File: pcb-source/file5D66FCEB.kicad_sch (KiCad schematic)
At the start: 9 parts, among them J5 Conn_01x02_Female, U3 AZ1117-5.0, U7 AMS1117-3.3, U8 AMS1117-1.8

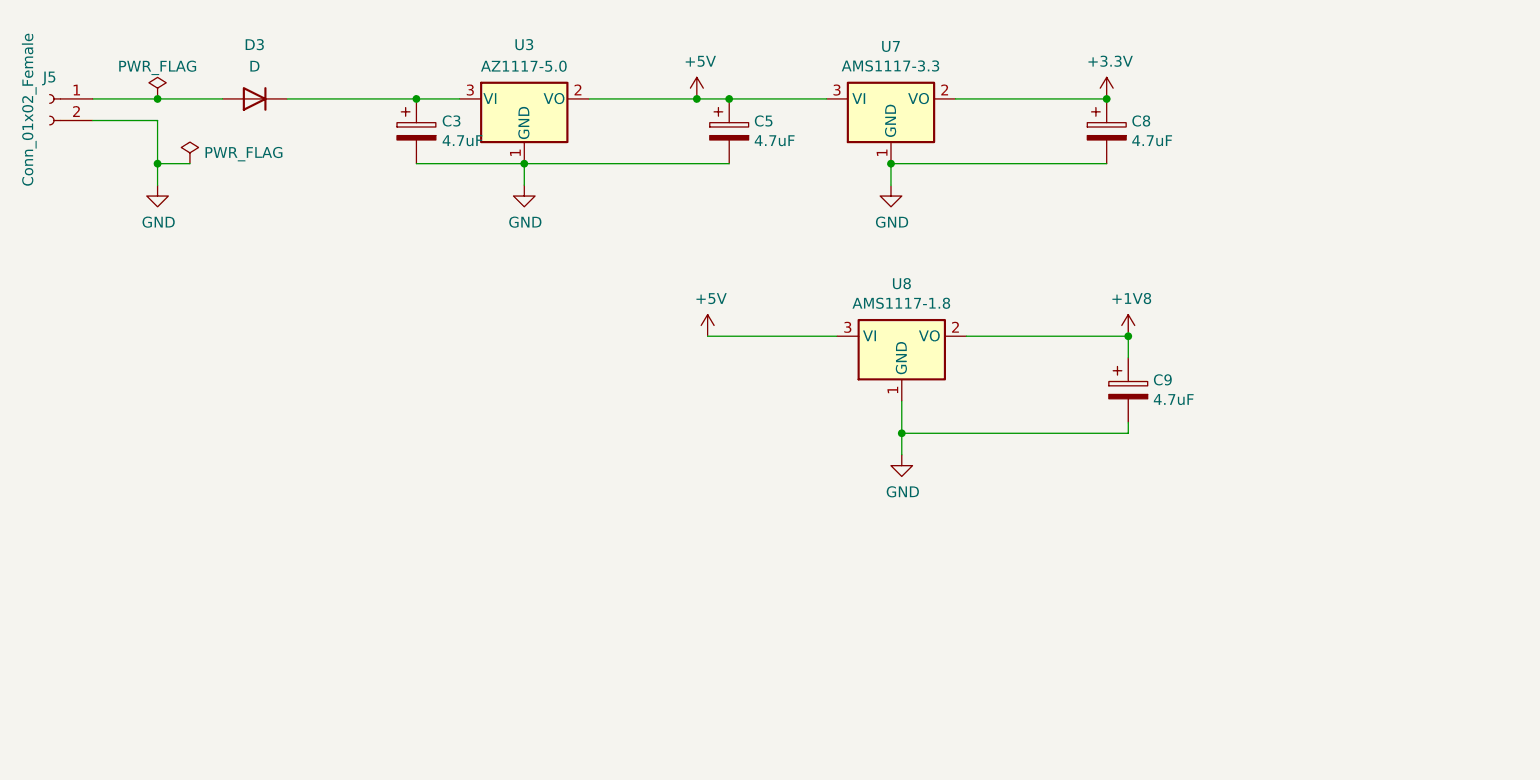
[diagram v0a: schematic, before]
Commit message: 1.2 version with 2 SPI buses
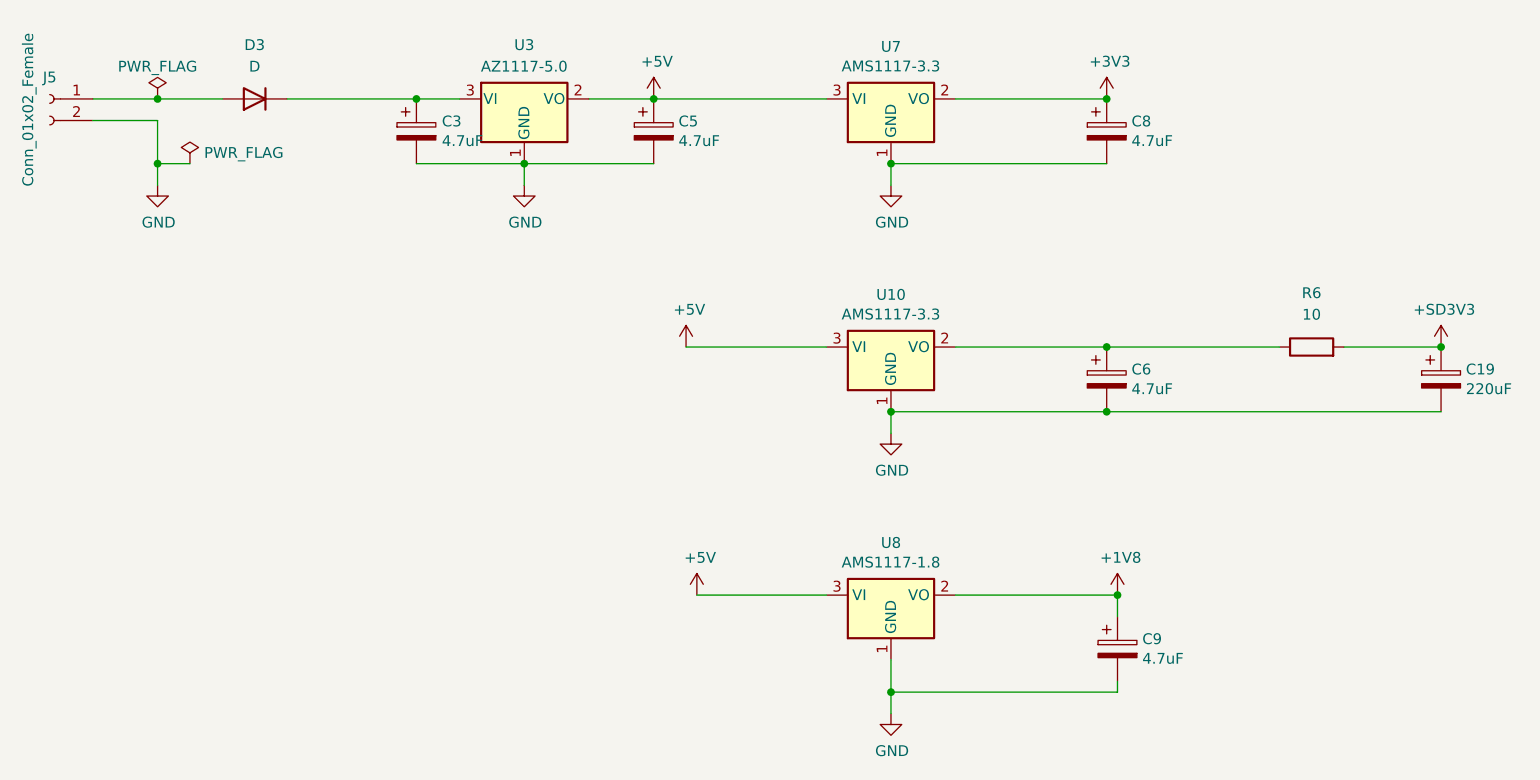
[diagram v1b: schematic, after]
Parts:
- added C19: 220uF, Capacitor_THT:CP_Radial_D6.3mm_P2.50mm, symbol AtariHDisk4-rescue:CP-Device
- added C6: 4.7uF, Capacitor_SMD:C_1206_3216Metric, symbol AtariHDisk4-rescue:CP-Device
- added R6: 10, Resistor_SMD:R_0805_2012Metric, symbol Device:R
- added U10: AMS1117-3.3, Package_TO_SOT_SMD:SOT-223-3_TabPin2, symbol Regulator_Linear:AMS1117-3.3
- C3: footprint Capacitor_THT:CP_Radial_D5.0mm_P2.00mm -> Capacitor_THT:CP_Radial_D6.3mm_P2.50mm
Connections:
- net +5V: now also U10.3 (VI)
- net GND: now also C19.2, C6.2, U10.1 (GND)
- new net: C6.1, R6.1, U10.2 (VO)
- new net +SD3V3: C19.1, R6.2
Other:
- moved on the sheet: C5, C9, U8
